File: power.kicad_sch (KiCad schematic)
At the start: 27 parts, among them U201 L78L33_SOT89, U202 AP62250

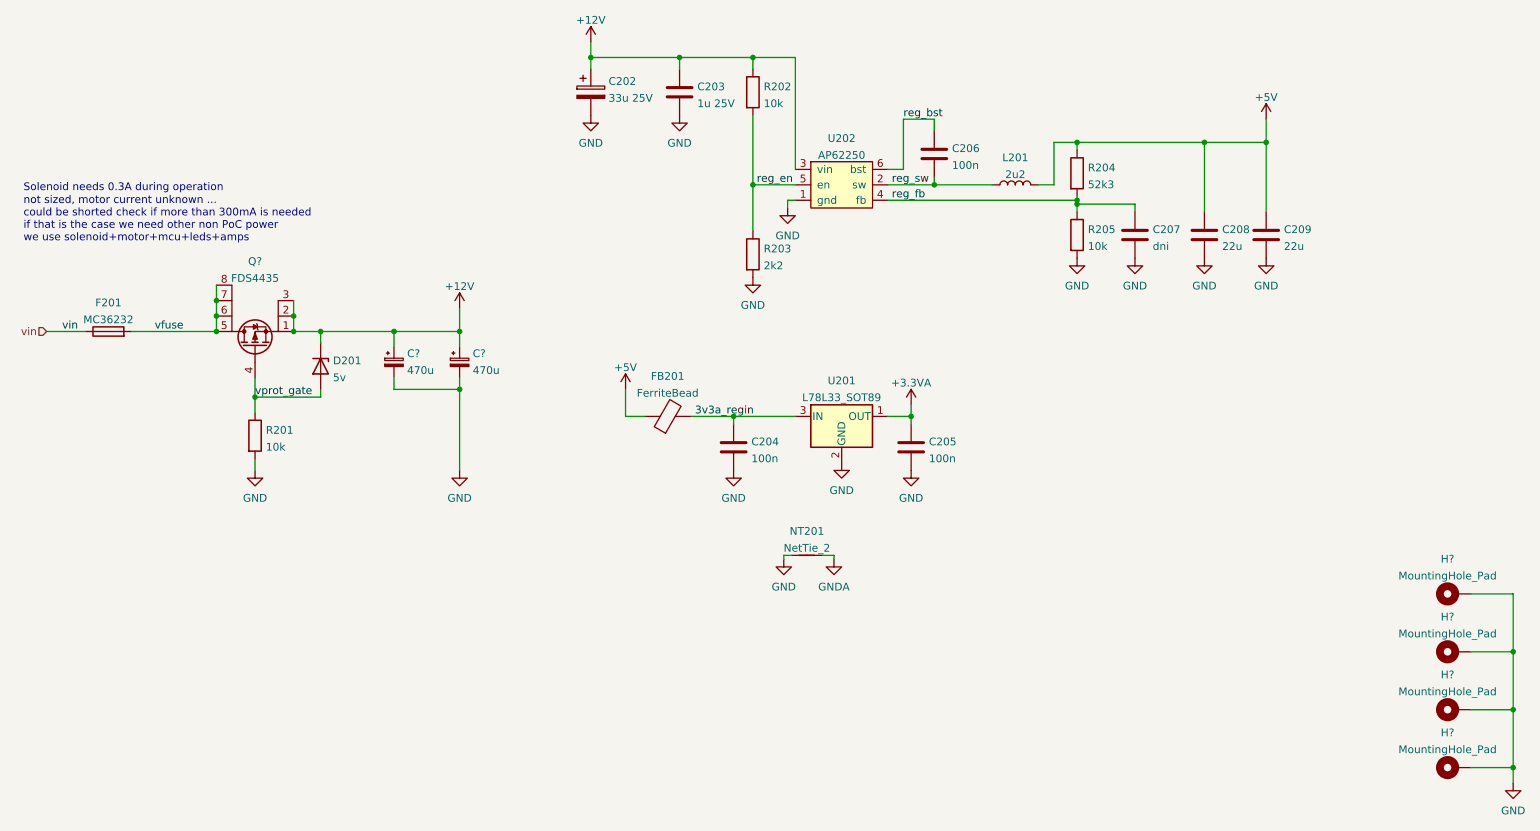
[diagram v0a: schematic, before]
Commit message: some form of schematic done, still lots to test
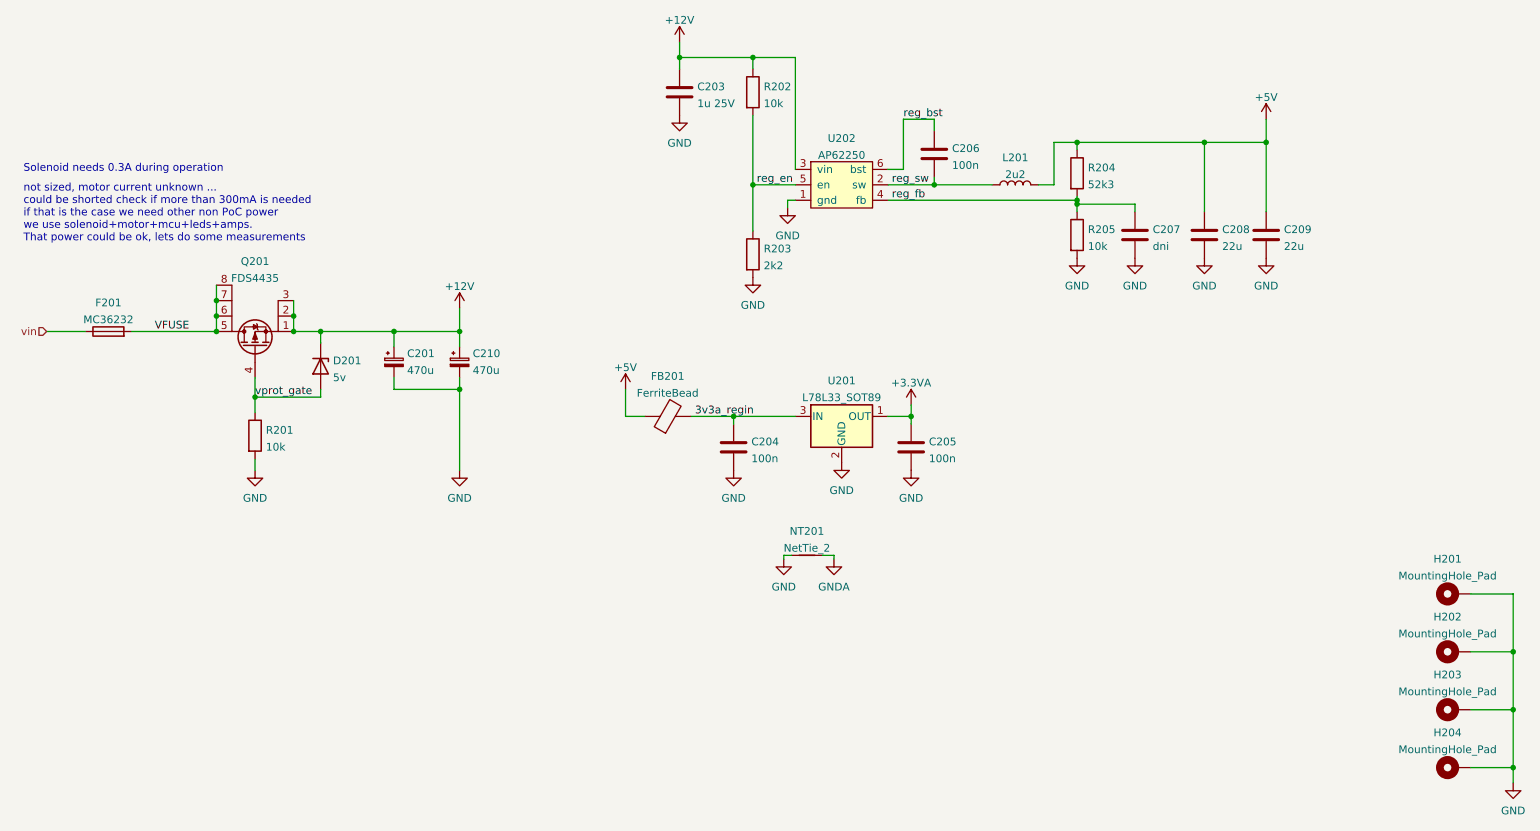
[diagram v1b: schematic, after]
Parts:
- removed C202: 33u 25V, symbol Device:C_Polarized
- C203: footprint (none) -> Capacitor_SMD:C_0603_1608Metric_Pad1.08x0.95mm_HandSolder
- D201: footprint (none) -> Diode_THT:D_DO-15_P2.54mm_Vertical_AnodeUp
- F201: footprint (none) -> Fuse:Fuse_1812_4532Metric
- U202: footprint (none) -> Package_TO_SOT_SMD:TSOT-23-6
- gave numbers to parts that had none: 7
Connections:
- net vfuse renamed VFUSE
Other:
- note added: "not sized, motor current unknown ... could be shorted check if more than 300mA is needed if that is the case we need other non PoC power we use solenoid+motor+mcu+leds+amps. That power could be ok, lets do some measurements"
- note removed: "not sized, motor current unknown ... could be shorted check if more than 300mA is needed if that is the case we need other non PoC power we use solenoid+motor+mcu+leds+amps"
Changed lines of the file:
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@@
   (junction (at 151.13 54.61) (diameter 0) (color 0 0 0 0)
   )
-  (junction (at 124.46 33.655) (diameter 0) (color 0 0 0 0)
-  )
   (junction (at 102.87 78.74) (diameter 0) (color 0 0 0 0)
   )
@@
     (stroke (width 0) (type default) (color 0 0 0 0))
   )
-  (wire (pts (xy 124.46 33.655) (xy 124.46 35.56))
-    (stroke (width 0) (type default) (color 0 0 0 0))
-  )
   (wire (pts (xy 80.01 78.74) (xy 80.01 80.645))
     (stroke (width 0) (type default) (color 0 0 0 0))
@@
     (stroke (width 0) (type default) (color 0 0 0 0))
   )
-  (wire (pts (xy 139.065 33.655) (xy 124.46 33.655))
-    (stroke (width 0) (type default) (color 0 0 0 0))
-  )
   (wire (pts (xy 200.66 54.61) (xy 200.66 47.625))
     (stroke (width 0) (type default) (color 0 0 0 0))
@@
     (stroke (width 0) (type default) (color 0 0 0 0))
   )
-  (wire (pts (xy 124.46 31.115) (xy 124.46 33.655))
+  (wire (pts (xy 139.065 31.115) (xy 139.065 33.655))
     (stroke (width 0) (type default) (color 0 0 0 0))
   )
@@
     (stroke (width 0) (type default) (color 0 0 0 0))
   )
-  (text "not sized, motor current unknown ... \ncould be shorted check if more than 300mA is needed\nif that is the case we need other non PoC power\nwe use solenoid+motor+mcu+leds+amps"
+  (text "not sized, motor current unknown ... \ncould be shorted check if more than 300mA is needed\nif that is the case we need other non PoC power\nwe use solenoid+motor+mcu+leds+amps.\nThat power could be ok, lets do some measurements"
     (at 31.115 64.135 0)
     (effects (font (size 1.27 1.27)) (justify left bottom))
   )
-  (text "Solenoid needs 0.3A during operation" (at 31.115 55.88 0)
+  (text "Solenoid needs 0.3A during operation" (at 31.115 52.705 0)
     (effects (font (size 1.27 1.27)) (justify left bottom))
   )
@@
     (effects (font (size 1.27 1.27)) (justify left bottom))
   )
-  (label "vin" (at 37.465 78.74 0)
-    (effects (font (size 1.27 1.27)) (justify left bottom))
-  )
   (label "3v3a_regin" (at 141.605 92.71 0)
     (effects (font (size 1.27 1.27)) (justify left bottom))
@@
     (effects (font (size 1.27 1.27)) (justify left bottom))
   )
-  (label "vfuse" (at 52.705 78.74 0)
+  (label "VFUSE" (at 52.705 78.74 0)
     (effects (font (size 1.27 1.27)) (justify left bottom))
   )
@@
     (pin "2")
   )
-  (symbol (lib_id "power:+12V") (at 124.46 31.115 0) (unit 1)
-    (in_bom yes) (on_board yes) (fields_autoplaced)
-    (property "Reference" "#PWR0104" (id 0) (at 124.46 34.925 0)
-      (effects (font (size 1.27 1.27)) hide)
-    )
-    (property "Value" "+12V" (id 1) (at 124.46 27.5105 0))
-    (property "Footprint" "" (id 2) (at 124.46 31.115 0)
-      (effects (font (size 1.27 1.27)) hide)
-    )
-    (property "Datasheet" "" (id 3) (at 124.46 31.115 0)
+  (symbol (lib_id "power:+12V") (at 139.065 31.115 0) (unit 1)
+    (in_bom yes) (on_board yes) (fields_autoplaced)
+    (property "Reference" "#PWR0104" (id 0) (at 139.065 34.925 0)
+      (effects (font (size 1.27 1.27)) hide)
+    )
+    (property "Value" "+12V" (id 1) (at 139.065 27.5105 0))
+    (property "Footprint" "" (id 2) (at 139.065 31.115 0)
+      (effects (font (size 1.27 1.27)) hide)
+    )
+    (property "Datasheet" "" (id 3) (at 139.065 31.115 0)
       (effects (font (size 1.27 1.27)) hide)
     )
@@
   (symbol (lib_id "Mechanical:MountingHole_Pad") (at 266.7 150.495 90) (unit 1)
     (in_bom yes) (on_board yes) (fields_autoplaced)
-    (property "Reference" "H?" (id 0) (at 265.43 144.7505 90))
+    (property "Reference" "H204" (id 0) (at 265.43 144.7505 90))
     (property "Value" "MountingHole_Pad" (id 1) (at 265.43 147.5256 90))
     (property "Footprint" "MountingHole:MountingHole_3.2mm_M3_DIN965_Pad" (id 2) (at 266.7 150.495 0)
@@
   (symbol (lib_id "Mechanical:MountingHole_Pad") (at 266.7 121.92 90) (unit 1)
     (in_bom yes) (on_board yes) (fields_autoplaced)
-    (property "Reference" "H?" (id 0) (at 265.43 116.1755 90))
+    (property "Reference" "H201" (id 0) (at 265.43 116.1755 90))
     (property "Value" "MountingHole_Pad" (id 1) (at 265.43 118.9506 90))
     (property "Footprint" "MountingHole:MountingHole_3.2mm_M3_DIN965_Pad" (id 2) (at 266.7 121.92 0)
@@
   (symbol (lib_id "good_things:Q_PMOS_SSSGDDDD") (at 69.215 81.28 90) (unit 1)
     (in_bom yes) (on_board yes) (fields_autoplaced)
-    (property "Reference" "Q?" (id 0) (at 69.215 67.2043 90))
+    (property "Reference" "Q201" (id 0) (at 69.215 67.2043 90))
     (property "Value" "FDS4435" (id 1) (at 69.215 69.9794 90))
     (property "Footprint" "Package_SO:SO-8_3.9x4.9mm_P1.27mm" (id 2) (at 66.675 76.2 0)
@@
       (effects (font (size 1.27 1.27)) (justify left))
     )
-    (property "Footprint" "" (id 2) (at 80.01 84.455 0)
+    (property "Footprint" "Diode_THT:D_DO-15_P2.54mm_Vertical_AnodeUp" (id 2) (at 80.01 84.455 0)
       (effects (font (size 1.27 1.27)) hide)
     )
@@
       (effects (font (size 1.27 1.27)) (justify left))
     )
-    (property "Footprint" "" (id 2) (at 140.0302 43.18 0)
+    (property "Footprint" "Capacitor_SMD:C_0603_1608Metric_Pad1.08x0.95mm_HandSolder" (id 2) (at 140.0302 43.18 0)
       (effects (font (size 1.27 1.27)) hide)
     )
@@
     (pin "1")
     (pin "2")
-  )
-  (symbol (lib_id "power:GND") (at 124.46 43.18 0) (unit 1)
-    (in_bom yes) (on_board yes) (fields_autoplaced)
-    (property "Reference" "#PWR0103" (id 0) (at 124.46 49.53 0)
-      (effects (font (size 1.27 1.27)) hide)
-    )
-    (property "Value" "GND" (id 1) (at 124.46 47.7425 0))
-    (property "Footprint" "" (id 2) (at 124.46 43.18 0)
-      (effects (font (size 1.27 1.27)) hide)
-    )
-    (property "Datasheet" "" (id 3) (at 124.46 43.18 0)
-      (effects (font (size 1.27 1.27)) hide)
-    )
-    (pin "1")
   )
   (symbol (lib_id "power:GNDA") (at 164.465 116.205 0) (unit 1)
@@
   (symbol (lib_id "Mechanical:MountingHole_Pad") (at 266.7 140.97 90) (unit 1)
     (in_bom yes) (on_board yes) (fields_autoplaced)
-    (property "Reference" "H?" (id 0) (at 265.43 135.2255 90))
+    (property "Reference" "H203" (id 0) (at 265.43 135.2255 90))
     (property "Value" "MountingHole_Pad" (id 1) (at 265.43 138.0006 90))
     (property "Footprint" "MountingHole:MountingHole_3.2mm_M3_DIN965_Pad" (id 2) (at 266.7 140.97 0)
@@
     (pin "1")
   )
-  (symbol (lib_id "Device:C_Polarized") (at 124.46 39.37 0) (unit 1)
-    (in_bom yes) (on_board yes) (fields_autoplaced)
-    (property "Reference" "C202" (id 0) (at 127.381 37.5725 0)
-      (effects (font (size 1.27 1.27)) (justify left))
-    )
-    (property "Value" "33u 25V" (id 1) (at 127.381 40.3476 0)
-      (effects (font (size 1.27 1.27)) (justify left))
-    )
-    (property "Footprint" "" (id 2) (at 125.4252 43.18 0)
-      (effects (font (size 1.27 1.27)) hide)
-    )
-    (property "Datasheet" "~" (id 3) (at 124.46 39.37 0)
-      (effects (font (size 1.27 1.27)) hide)
-    )
-    (pin "1")
-    (pin "2")
-  )
   (symbol (lib_id "Device:C_Polarized_Small") (at 102.87 83.82 0) (unit 1)
     (in_bom yes) (on_board yes) (fields_autoplaced)
-    (property "Reference" "C?" (id 0) (at 105.029 82.3654 0)
+    (property "Reference" "C210" (id 0) (at 105.029 82.3654 0)
       (effects (font (size 1.27 1.27)) (justify left))
     )
@@
     (property "Reference" "F201" (id 0) (at 45.085 74.0115 90))
     (property "Value" "MC36232" (id 1) (at 45.085 76.7866 90))
-    (property "Footprint" "" (id 2) (at 45.085 80.518 90)
+    (property "Footprint" "Fuse:Fuse_1812_4532Metric" (id 2) (at 45.085 80.518 90)
       (effects (font (size 1.27 1.27)) hide)
     )
@@
   (symbol (lib_id "Device:C_Polarized_Small") (at 92.075 83.82 0) (unit 1)
     (in_bom yes) (on_board yes) (fields_autoplaced)
-    (property "Reference" "C?" (id 0) (at 94.234 82.3654 0)
+    (property "Reference" "C201" (id 0) (at 94.234 82.3654 0)
       (effects (font (size 1.27 1.27)) (justify left))
     )
@@
   (symbol (lib_id "Mechanical:MountingHole_Pad") (at 266.7 131.445 90) (unit 1)
     (in_bom yes) (on_board yes) (fields_autoplaced)
-    (property "Reference" "H?" (id 0) (at 265.43 125.7005 90))
+    (property "Reference" "H202" (id 0) (at 265.43 125.7005 90))
     (property "Value" "MountingHole_Pad" (id 1) (at 265.43 128.4756 90))
     (property "Footprint" "MountingHole:MountingHole_3.2mm_M3_DIN965_Pad" (id 2) (at 266.7 131.445 0)
@@
     (property "Reference" "U202" (id 0) (at 165.735 46.9605 0))
     (property "Value" "AP62250" (id 1) (at 165.735 49.7356 0))
-    (property "Footprint" "" (id 2) (at 165.735 55.88 0)
+    (property "Footprint" "Package_TO_SOT_SMD:TSOT-23-6" (id 2) (at 165.735 55.88 0)
       (effects (font (size 1.27 1.27)) hide)
     )
@@
   (symbol (lib_id "power:GND") (at 276.225 153.035 0) (unit 1)
     (in_bom yes) (on_board yes) (fields_autoplaced)
-    (property "Reference" "#PWR?" (id 0) (at 276.225 159.385 0)
-      (effects (font (size 1.27 1.27)) hide)
-    )
+    (property "Reference" "#PWR0201" (id 0) (at 276.225 159.385 0)
+      (effects (font (size 1.27 1.27)) hide)
+    )
